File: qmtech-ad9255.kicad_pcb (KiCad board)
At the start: 4 copper layers, 70 x 90 mm, 85 parts

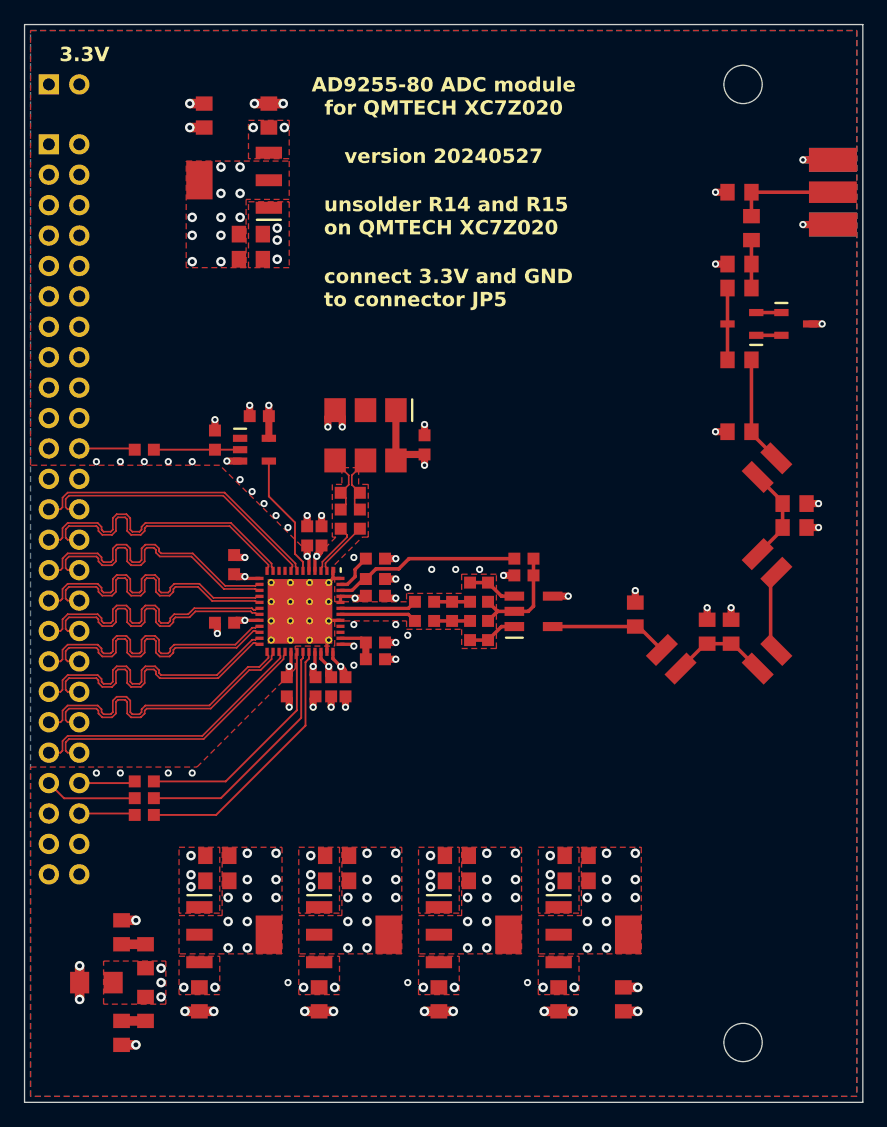
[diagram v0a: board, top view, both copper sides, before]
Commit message: add thermal reliefs to all zones in qmtech-ad9255
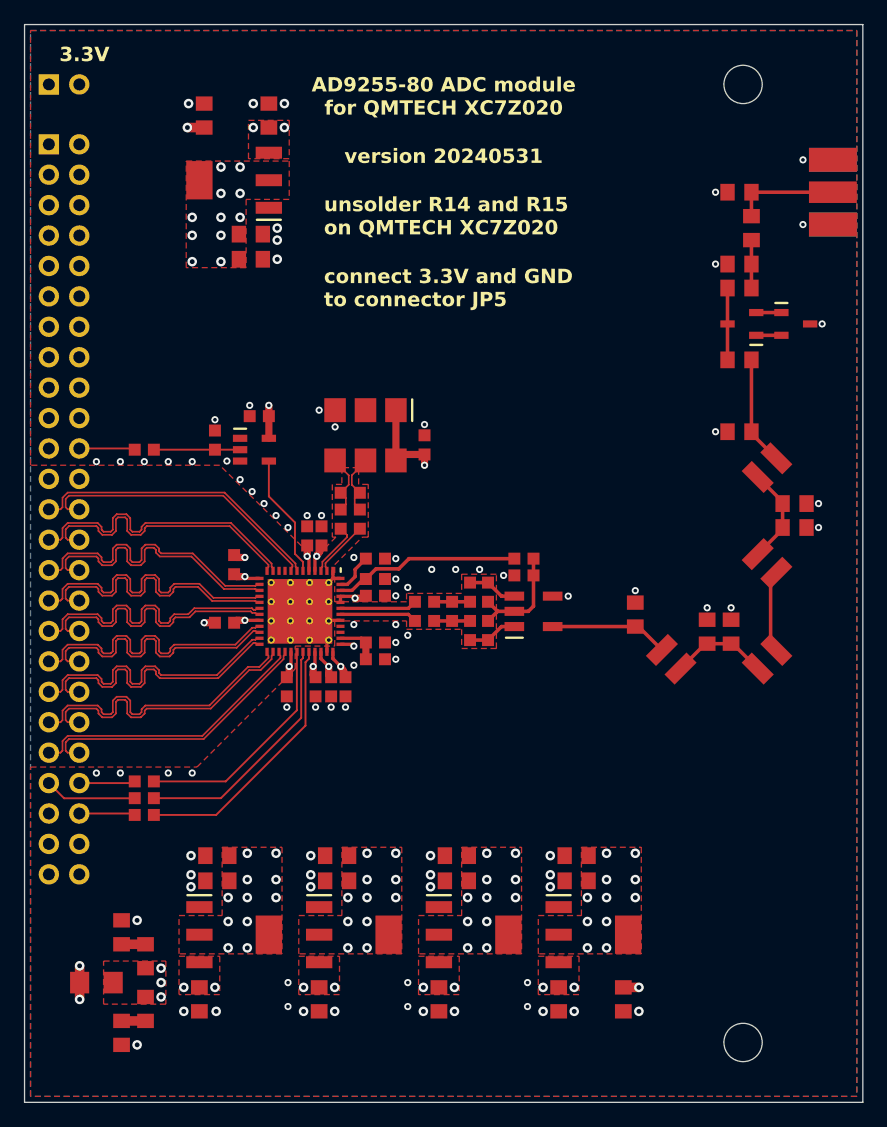
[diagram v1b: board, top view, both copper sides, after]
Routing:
- net GND: track 62.3 -> 6.95 mm, vias 88 -> 91
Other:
- board text added: "version 20240531"
- board text removed: "version 20240527"

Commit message: increase size of zones under regulators in qmtech-ad9255
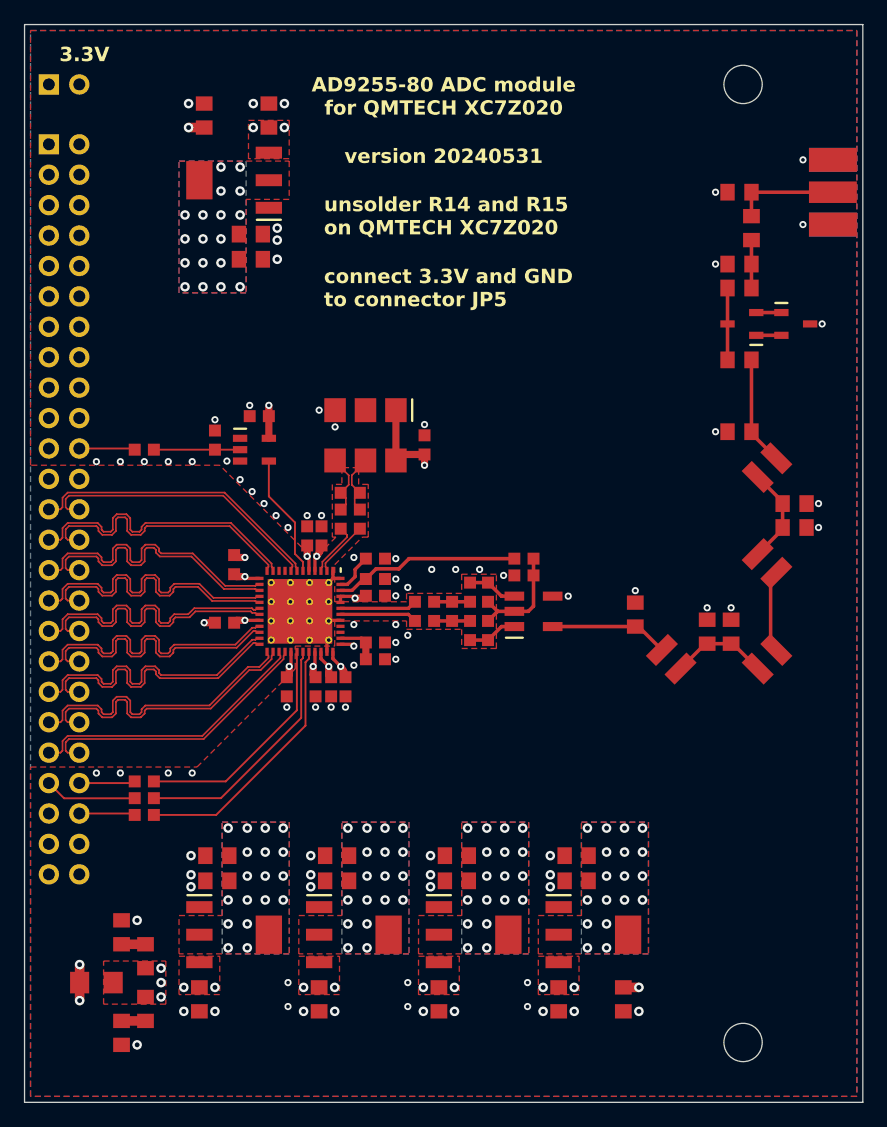
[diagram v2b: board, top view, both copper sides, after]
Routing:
- net VCCO25: vias 11 -> 18
- net SVDD: vias 12 -> 19
- net DVDD: vias 15 -> 22
- net CVDD: vias 12 -> 19
- net AVDD: vias 16 -> 23
- added copper zone on B.Cu, net AVDD
- added copper zone on B.Cu, net CVDD
- added copper zone on B.Cu, net DVDD
- added copper zone on B.Cu, net SVDD
- added copper zone on B.Cu, net VCCO25

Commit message: move VIN1 and 5V zones to front layer in qmtech-ad9255
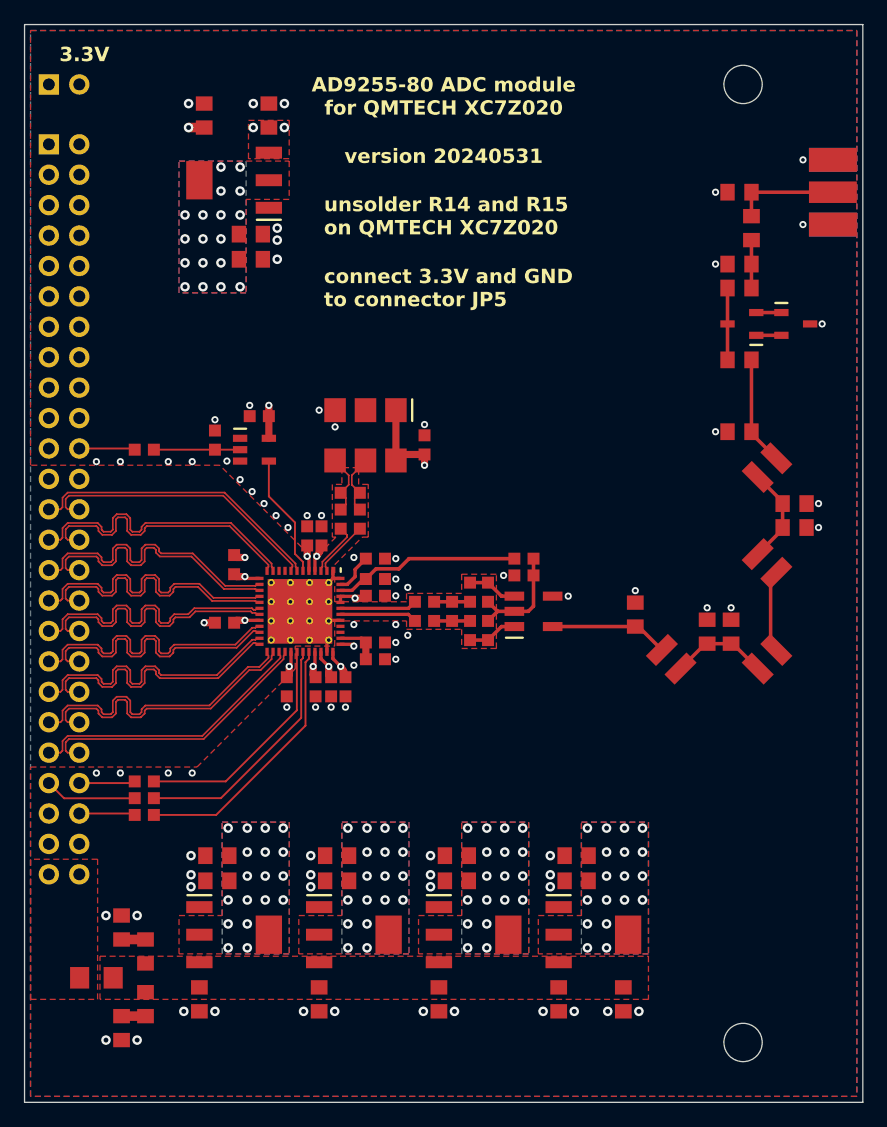
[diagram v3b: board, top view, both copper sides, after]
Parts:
- moved FB1 0.40 mm to (116.0, 129.6)
- moved C29 0.40 mm to (120.1, 127.4)
- moved R16 0.40 mm to (118.1, 125.4)
- moved C28 0.40 mm to (120.1, 131.8)
- moved R15 0.40 mm to (118.1, 133.8)
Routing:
- net VIN1: track 3.00 -> 0.00 mm, vias 2 -> 0
- net 5V: track 1.30 -> 0.00 mm, vias 12 -> 0
- net GND: vias 91 -> 84
- added copper zone on F.Cu, net VIN1
- removed copper zone on In2.Cu, net 5V
- removed copper zone on In2.Cu, net VIN1

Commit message: add GND vias to qmtech-ad9255
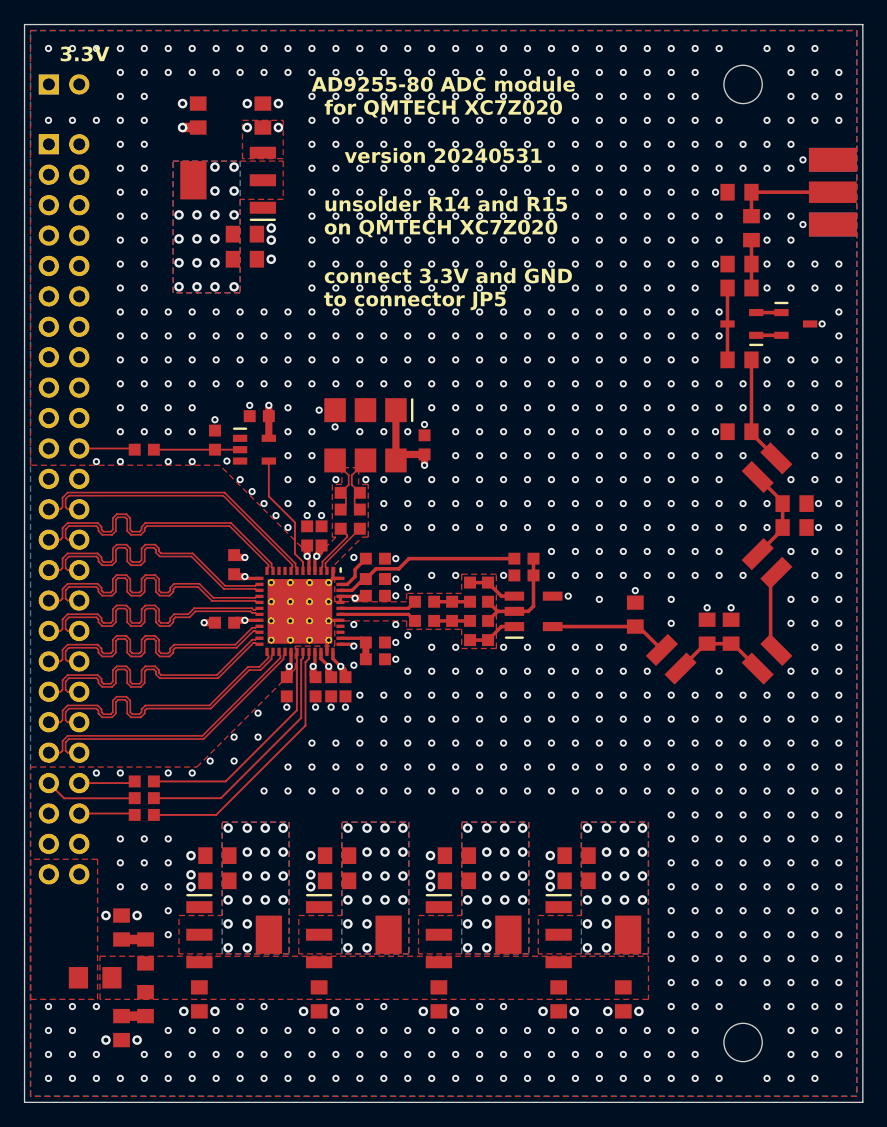
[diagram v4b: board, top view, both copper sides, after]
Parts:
- moved C26 0.50 mm to (129.9, 57.6)
- moved C27 0.50 mm to (128.4, 67.5)
- moved IC6 0.50 mm to (127.0, 63.0)
- moved R22 0.50 mm to (124.5, 57.6)
- moved R23 0.50 mm to (128.4, 69.6)
- moved FB1 0.10 mm to (115.9, 129.6)
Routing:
- net GND: vias 84 -> 944

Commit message: improve power planes in qmtech-ad9255
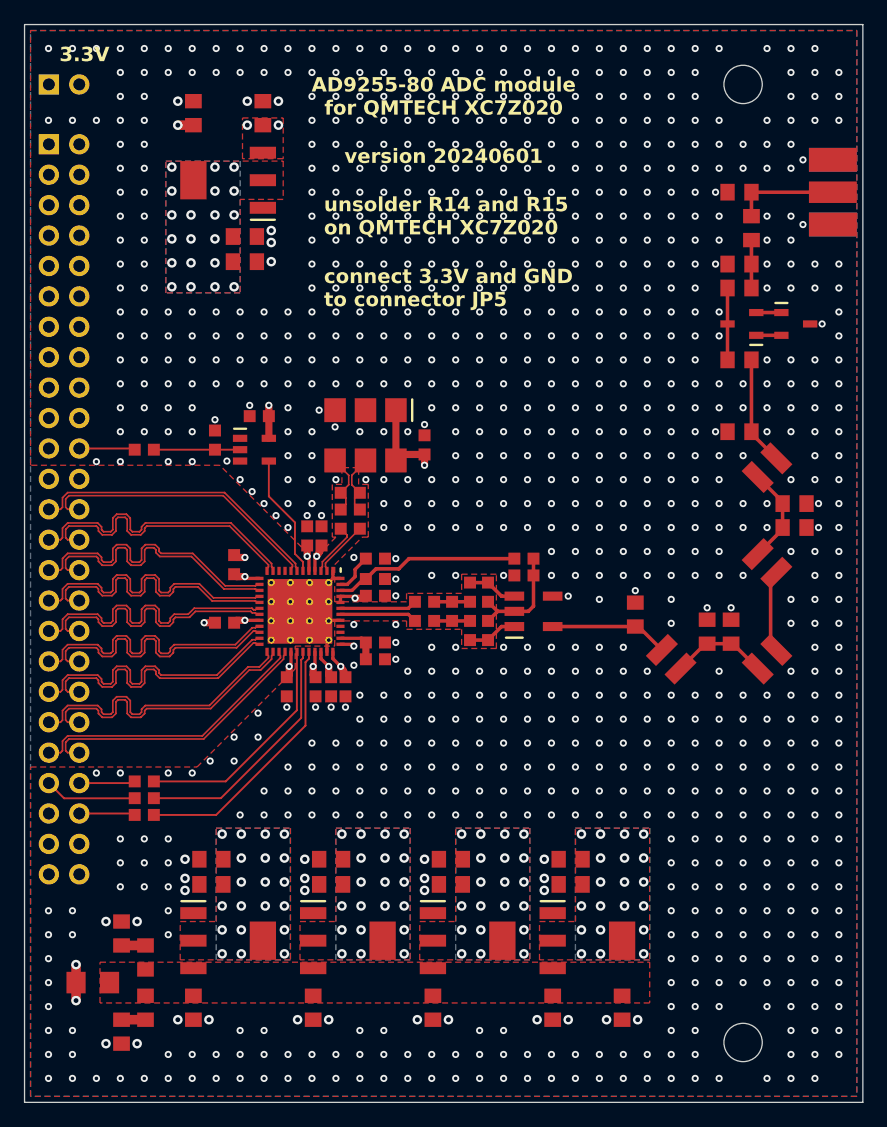
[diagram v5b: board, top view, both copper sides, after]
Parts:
- moved C18 0.86 mm to (124.1, 132.1)
- moved C20 0.86 mm to (134.1, 132.1)
- moved C22 0.86 mm to (144.1, 132.1)
- moved C24 0.86 mm to (154.1, 132.1)
- moved IC2 0.71 mm to (127.0, 126.5)
- moved IC3 0.71 mm to (137.0, 126.5)
- moved IC4 0.71 mm to (147.0, 126.5)
- moved IC5 0.71 mm to (157.0, 126.5)
- moved R17 0.71 mm to (159.9, 132.1)
- moved C19 0.58 mm to (125.6, 121.8)
- moved C21 0.58 mm to (135.6, 121.8)
- moved C23 0.58 mm to (145.6, 121.8)
- moved C25 0.58 mm to (155.6, 121.8)
- moved R18 0.58 mm to (125.6, 119.7)
- moved R19 0.58 mm to (135.6, 119.7)
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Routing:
- net VIN1: track 0.00 -> 3.00 mm, vias 0 -> 2
- net VCCO25: vias 18 -> 20
- net SVDD: vias 19 -> 21
- net GND: vias 944 -> 941
- net DVDD: vias 22 -> 24
- net CVDD: vias 19 -> 21
- net AVDD: vias 23 -> 25
- added copper zone on In2.Cu, net VIN1
- removed copper zone on F.Cu, net VIN1
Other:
- board text added: "version 20240601"
- board text removed: "version 20240531"

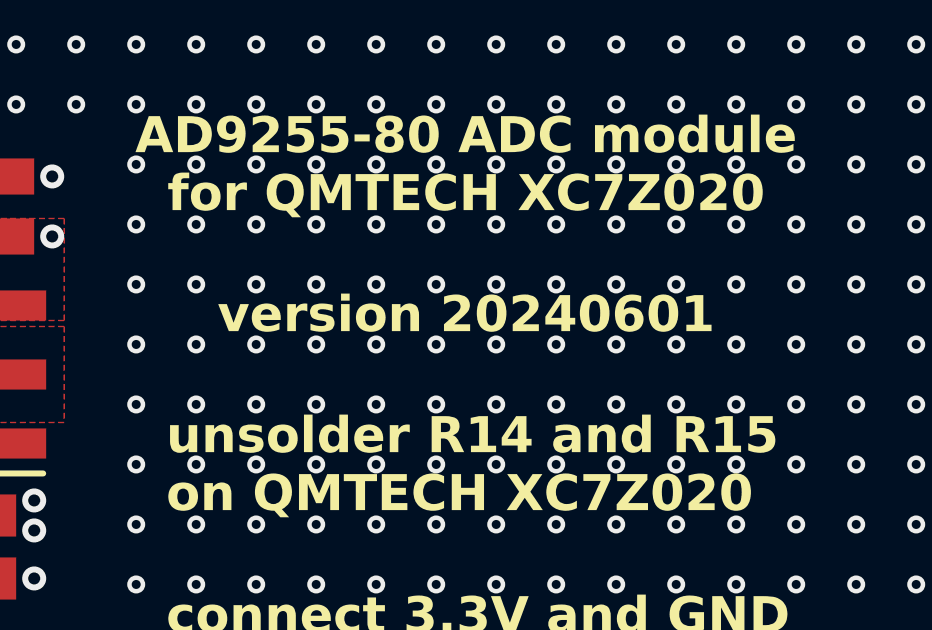
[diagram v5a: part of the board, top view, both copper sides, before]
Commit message: set part number for R22 to C17414 in qmtech-ad9255
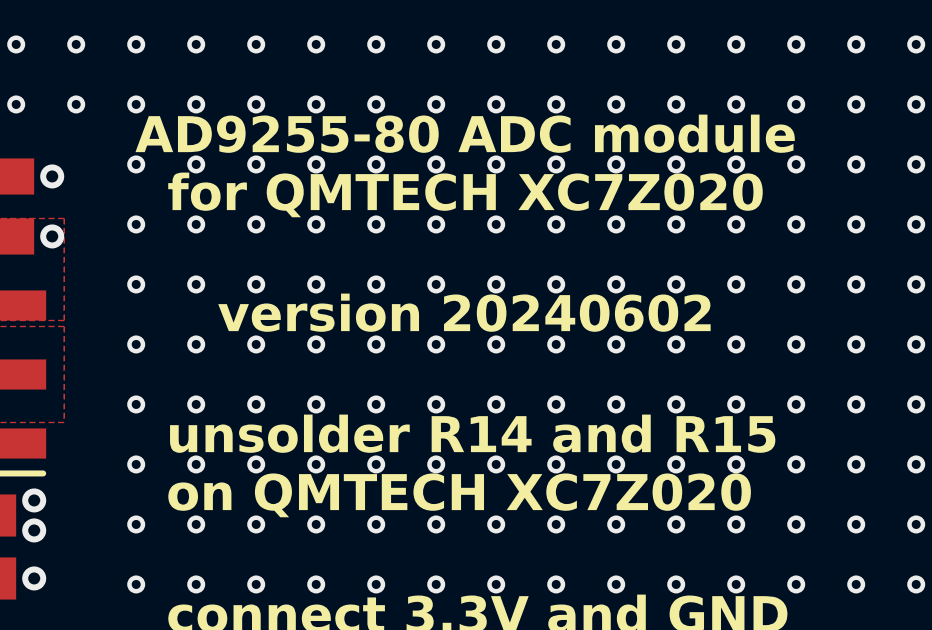
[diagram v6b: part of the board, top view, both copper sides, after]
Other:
- board text added: "version 20240602"
- board text removed: "version 20240601"
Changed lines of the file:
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@@
   (footprint "footprints:0805" (layer "F.Cu")
     (at 124.1 57.4 90)
-    (property "mpn" "C17513")
+    (property "mpn" "C17414")
     (attr smd)
     (fp_text reference "R22" (at 3.6 -0.1 90) (layer "F.SilkS") hide
@@
     (effects (font (size 1.2 1.2) (thickness 0.2) bold))
   )
-  (gr_text "version 20240601" (at 145 61) (layer "F.SilkS")
+  (gr_text "version 20240602" (at 145 61) (layer "F.SilkS")
     (effects (font (size 1.2 1.2) (thickness 0.2) bold))
   )

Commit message: reduce filter shield frame width in qmtech-ad9255
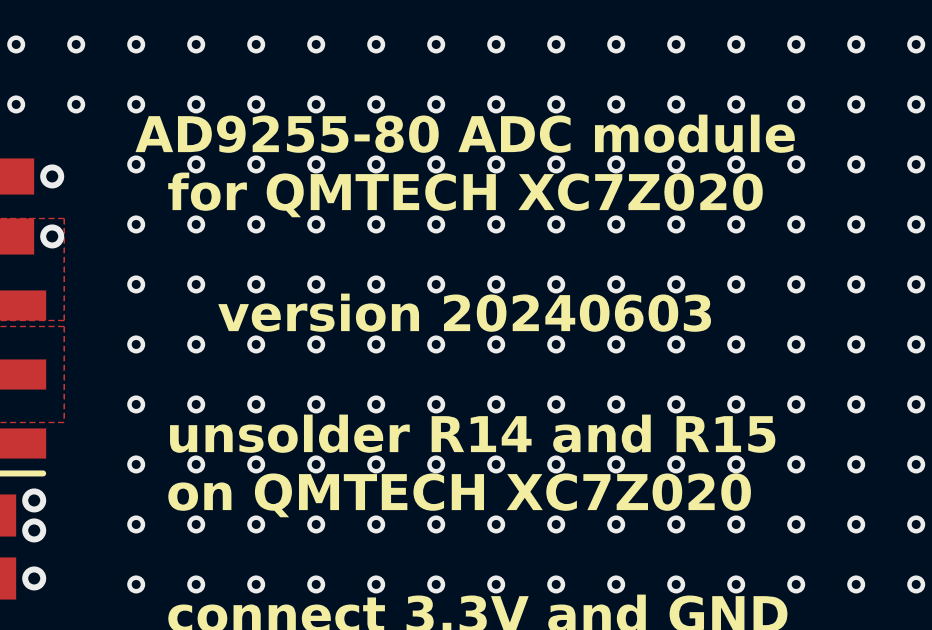
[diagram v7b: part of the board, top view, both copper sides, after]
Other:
- board text added: "version 20240603"
- board text removed: "version 20240602"
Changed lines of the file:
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@@
     (effects (font (size 1.2 1.2) (thickness 0.2) bold))
   )
-  (gr_text "version 20240602" (at 145 61) (layer "F.SilkS")
+  (gr_text "version 20240603" (at 145 61) (layer "F.SilkS")
     (effects (font (size 1.2 1.2) (thickness 0.2) bold))
   )
@@
     (polygon
       (pts
-        (xy 170.3 82)
+        (xy 170.3 81.5)
         (xy 170.3 80.5)
         (xy 157.5 80.5)
         (xy 157.5 99.87)
-        (xy 159 99.87)
-        (xy 159 82)
+        (xy 158.5 99.87)
+        (xy 158.5 81.5)
       )
     )
@@
     (polygon
       (pts
-        (xy 171.1 82)
+        (xy 171.1 81.5)
         (xy 171.1 80.5)
-        (xy 179 80.5)
-        (xy 179 108)
-        (xy 157.5 108)
+        (xy 178.5 80.5)
+        (xy 178.5 108.5)
+        (xy 157.5 108.5)
         (xy 157.5 100.67)
-        (xy 159 100.67)
-        (xy 159 106.5)
-        (xy 177.5 106.5)
-        (xy 177.5 82)
-      )
-    )
+        (xy 158.5 100.67)
+        (xy 158.5 107.5)
+        (xy 177.5 107.5)
+        (xy 177.5 81.5)
+      )
+    )

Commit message: update version in qmtech-ad9255
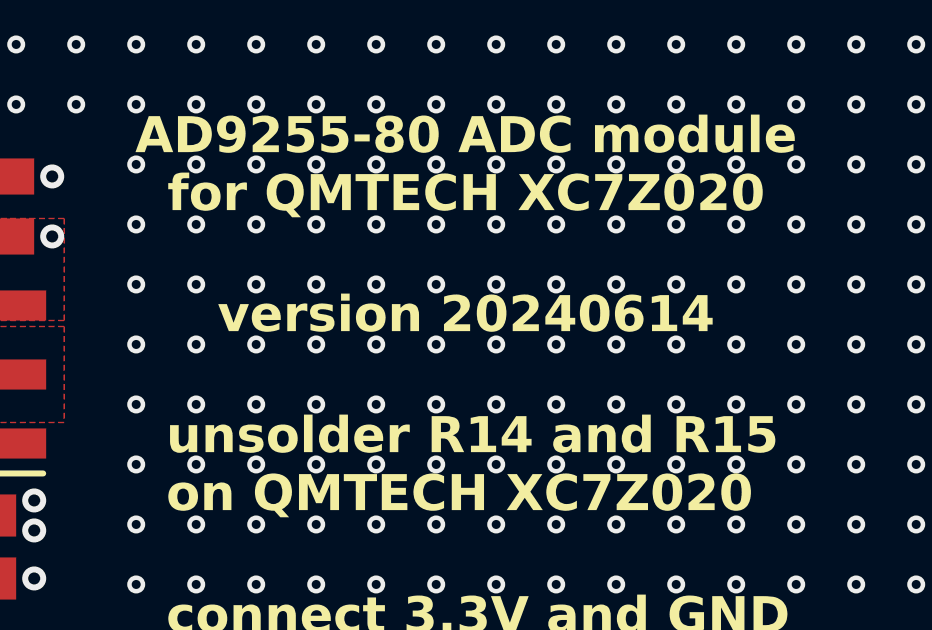
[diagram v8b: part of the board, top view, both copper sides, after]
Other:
- board text added: "version 20240614"
- board text removed: "version 20240603"
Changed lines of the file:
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@@
     (effects (font (size 1.2 1.2) (thickness 0.2) bold))
   )
-  (gr_text "version 20240603" (at 145 61) (layer "F.SilkS")
+  (gr_text "version 20240614" (at 145 61) (layer "F.SilkS")
     (effects (font (size 1.2 1.2) (thickness 0.2) bold))
   )
